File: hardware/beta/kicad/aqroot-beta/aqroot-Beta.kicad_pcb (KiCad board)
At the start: 4 copper layers, 74 x 155 mm, 188 parts, among them J1 CH280QV10-CT_50P, J2 Molex_5025700893, J3 USB_C_Receptacle_USB2.0_16P, J4 JST-PH-2 BATTERY, J5 COMMUNITY_HEADER_2x13, J6 JST-PH-2 SPEAKER, Q1 AO3400A, SW1 BOOT, SW2 UP, SW3 DOWN, SW4 LEFT, SW5 RIGHT, SW6 A_SELECT, SW7 B_BACK, SW8 HOME, SW9 SW_SPDT, U1 ESP32-S3-WROOM-1, U10 USBLC6-2SC6, U11 BQ25185, U12 TPS63020, U13 TPS61023, U14 MAX17048, U15 TPS22918, U16 TCA9517ADGK, U17 TPS61169DCKR, U2 TCA9535PWR, U3 TCA9535PWR, U4 BMI270, U5 MAX98357A, U6 TSOP38238, U7 E07-400M10S, U8 E22-900M22S, U9 ST25R3916-AQET

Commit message: route SX1262_RST_N from U2.5
Closes SX1262_RST_N: one island over U2.5, R13.1 and U8.15, 159.325 mm of
new copper in 17 tracks and 7 vias across In2 9 / B.Cu 8 / F.Cu 1. Board
ratsnest 414 -> 411, DRC 0 electrical errors. E5 x65 consumed in place.

The north-window architecture from the previous analysis pass held. The
source leaves U2.5 west on B.Cu, dives to In2 at x 13.700 to clear the
WAKE_INT_N B.Cu wall, returns to B.Cu at y 52.000 for the R13 pull-down
tee at x 17.375, hops F.Cu across x 23..30, then runs In2 east to x 57
and north to y 38.000. The band crossing is a B.Cu run at y 38.000 from
x 57 to x 71, well clear of both antenna bands, and the return descends
In2 down the east edge to meet the staged x65 crossing at y 85.000.
R13.2 is GND, so R13 is a pull-down tee and not a series element.

One correction to the audited geometry. The predicted 0.225 mm minimum
was scored against the 0.200 mm global clearance, but on the east lane
that gap falls against the USB_VBUS_CHG via at (70.775, 64.6), which
carries the elevated 0.250 mm VBUS_CHG routed clearance from .kicad_dru
section 10. At the audited x 71.500 the lane measured 0.225 mm and DRC
failed on exactly that one pair. The lane moved to x 71.600, the only
change against the audited route: the legal window is [71.525, 73.400]
and is empty of copper on In2 and of through vias, so the fix is a
0.100 mm lateral shift of three segments, not a new architecture. The
gap is now 0.325 mm and the board edge at x 74 is 2.300 mm away.

Actual minimum route clearance is 0.225 mm, at the x 13.700 y 52.000 via
against R10.1 on +3V3, where the requirement is the 0.200 mm global
figure. All four Edge.Cuts mounting cutouts were checked explicitly and
the nearest new copper is 12.082 mm from the hole at (70.5, 144.0).

RF audit: 0 new vias and 0 new outer-layer transit in either the 915 or
the 433 band, and no new In2 copper inside either band - the only in-band
copper on this net remains the pre-existing x65 segment, con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
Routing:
- net /SX1262_RST_N: track 32.0 -> 191.3 mm, vias 0 -> 7
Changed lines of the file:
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@@
 	(footprint "C_0603_1608Metric"
 		(layer "B.Cu")
-		(at 46.1 82.5)
+		(at 28.5 79 180)
 		(descr "Capacitor SMD 0603 (1608 Metric), square (rectangular) end terminal, IPC-7351 nominal, (Body size source: IPC-SM-782 page 76, https://www.pcb-3d.com/wordpress/wp-content/uploads/ipc-sm-782a_amendment_1_and_2.pdf)")
 		(tags "capacitor")
-		(property "Reference" "C56"
-			(at 0 1.43 180)
+		(property "Reference" "C13"
+			(at 0 1.43 0)
 			(layer "B.SilkS")
 			(effects
@@
 			)
 		)
-		(property "Value" "1uF"
-			(at 0 -1.43 180)
+		(property "Value" "100nF"
+			(at 0 -1.43 0)
 			(layer "B.Fab")
 			(effects
@@
 		)
 		(property "Datasheet" ""
-			(at 0 0 180)
+			(at 0 0 0)
 			(layer "B.Fab")
 			(hide yes)
@@
 		)
 		(property "Description" ""
-			(at 0 0 180)
+			(at 0 0 0)
 			(layer "B.Fab")
 			(hide yes)
@@
 		)
 		(property "KiLib_Generator" "SMD_2terminal_chip_molded"
-			(at 0 0 180)
+			(at 0 0 0)
 			(layer "B.SilkS")
 			(hide yes)
@@
 		(duplicate_pad_numbers_are_jumpers no)
 		(fp_line
-			(start -0.14058 -0.51)
-			(end 0.14058 -0.51)
+			(start -0.14058 0.51)
+			(end 0.14058 0.51)
 			(stroke
 				(width 0.12)
@@
 		)
 		(fp_line
-			(start -0.14058 0.51)
-			(end 0.14058 0.51)
+			(start -0.14058 -0.51)
+			(end 0.14058 -0.51)
 			(stroke
 				(width 0.12)
@@
 		)
 		(fp_text user "${REFERENCE}"
-			(at 0 0 180)
+			(at 0 0 0)
 			(layer "B.Fab")
 			(effects
@@
 		)
 		(pad "1" smd roundrect
-			(at -0.775 0)
+			(at -0.775 0 180)
 			(size 0.9 0.95)
 			(layers "B.Cu" "B.Mask" "B.Paste")
@@
 		)
 		(pad "2" smd roundrect
-			(at 0.775 0)
+			(at 0.775 0 180)
 			(size 0.9 0.95)
 			(layers "B.Cu" "B.Mask" "B.Paste")
@@
 	(footprint "C_0603_1608Metric"
 		(layer "B.Cu")
-		(at 28.5 79 180)
+		(at 46.1 82.5)
 		(descr "Capacitor SMD 0603 (1608 Metric), square (rectangular) end terminal, IPC-7351 nominal, (Body size source: IPC-SM-782 page 76, https://www.pcb-3d.com/wordpress/wp-content/uploads/ipc-sm-782a_amendment_1_and_2.pdf)")
 		(tags "capacitor")
-		(property "Reference" "C13"
-			(at 0 1.43 0)
+		(property "Reference" "C56"
+			(at 0 1.43 180)
 			(layer "B.SilkS")
 			(effects
@@
 			)
 		)
-		(property "Value" "100nF"
-			(at 0 -1.43 0)
+		(property "Value" "1uF"
+			(at 0 -1.43 180)
 			(layer "B.Fab")
 			(effects
@@
 		)
 		(property "Datasheet" ""
-			(at 0 0 0)
+			(at 0 0 180)
 			(layer "B.Fab")
 			(hide yes)
@@
 		)
 		(property "Description" ""
-			(at 0 0 0)
+			(at 0 0 180)
 			(layer "B.Fab")
 			(hide yes)
@@
 		)
 		(property "KiLib_Generator" "SMD_2terminal_chip_molded"
-			(at 0 0 0)
+			(at 0 0 180)
 			(layer "B.SilkS")
 			(hide yes)
@@
 		(duplicate_pad_numbers_are_jumpers no)
 		(fp_line
-			(start -0.14058 0.51)
-			(end 0.14058 0.51)
+			(start -0.14058 -0.51)
+			(end 0.14058 -0.51)
 			(stroke
 				(width 0.12)
@@
 		)
 		(fp_line
-			(start -0.14058 -0.51)
-			(end 0.14058 -0.51)
+			(start -0.14058 0.51)
+			(end 0.14058 0.51)
 			(stroke
 				(width 0.12)
@@
 		)
 		(fp_text user "${REFERENCE}"
-			(at 0 0 0)
+			(at 0 0 180)
 			(layer "B.Fab")
 			(effects
@@
 		)
 		(pad "1" smd roundrect
-			(at -0.775 0 180)
+			(at -0.775 0)
 			(size 0.9 0.95)
 			(layers "B.Cu" "B.Mask" "B.Paste")
@@
 		)
 		(pad "2" smd roundrect
-			(at 0.775 0 180)
+			(at 0.775 0)
 			(size 0.9 0.95)
 			(layers "B.Cu" "B.Mask" "B.Paste")
@@
 	)
 	(segment
+		(start 23 52)
+		(end 30 52)
+		(width 0.2)
+		(layer "F.Cu")
+		(net "/SX1262_RST_N")
+	)
+	(via
+		(at 13.7 48.35)
+		(size 0.6)
+		(drill 0.3)
+		(layers "F.Cu" "B.Cu")
+		(net "/SX1262_RST_N")
+	)
+	(via
+		(at 13.7 52)
+		(size 0.6)
+		(drill 0.3)
+		(layers "F.Cu" "B.Cu")
+		(net "/SX1262_RST_N")
+	)
+	(via
+		(at 23 52)
+		(size 0.6)
+		(drill 0.3)
+		(layers "F.Cu" "B.Cu")
+		(net "/SX1262_RST_N")
+	)
+	(via
+		(at 30 52)
+		(size 0.6)
+		(drill 0.3)
+		(layers "F.Cu" "B.Cu")
+		(net "/SX1262_RST_N")
+	)
+	(via
+		(at 57 38)
+		(size 0.6)
+		(drill 0.3)
+		(layers "F.Cu" "B.Cu")
+		(net "/SX1262_RST_N")
+	)
+	(via
+		(at 71 38)
+		(size 0.6)
+		(drill 0.3)
+		(layers "F.Cu" "B.Cu")
+		(net "/SX1262_RST_N")
+	)
+	(via
+		(at 65 131)
+		(size 0.6)
+		(drill 0.3)
+		(layers "F.Cu" "B.Cu")
+		(net "/SX1262_RST_N")
+	)
+	(segment
+		(start 9.7 44.975)
+		(end 11.5 44.975)
+		(width 0.2)
+		(layer "B.Cu")
+		(net "/SX1262_RST_N")
+	)
+	(segment
+		(start 11.5 44.975)
+		(end 11.5 48.35)
+		(width 0.2)
+		(layer "B.Cu")
+		(net "/SX1262_RST_N")
+	)
+	(segment
+		(start 11.5 48.35)
+		(end 13.7 48.35)
+		(width 0.2)
+		(layer "B.Cu")
+		(net "/SX1262_RST_N")
+	)
+	(segment
+		(start 13.7 52)
+		(end 23 52)
+		(width 0.2)
+		(layer "B.Cu")
+		(net "/SX1262_RST_N")
+	)
+	(segment
+		(start 17.375 52)
+		(end 17.375 53)
+		(width 0.2)
+		(layer "B.Cu")
+		(net "/SX1262_RST_N")
+	)
+	(segment
+		(start 57 38)
+		(end 71 38)
+		(width 0.2)
+		(layer "B.Cu")
+		(net "/SX1262_RST_N")
+	)
+	(segment
+		(start 65 131)
+		(end 65 131.8)
+		(width 0.2)
+		(layer "B.Cu")
+		(net "/SX1262_RST_N")
+	)
+	(segment
+		(start 65 131.8)
+		(end 58 131.8)
+		(width 0.2)
+		(layer "B.Cu")
+		(net "/SX1262_RST_N")
+	)
+	(segment
 		(start 65 85)
 		(end 65 117)
 		(width 0.2)
 		(layer "In2.Cu")
+		(net "/SX1262_RST_N")
+	)
+	(segment
+		(start 13.7 48.35)
+		(end 13.7 52)
+		(width 0.2)
+		(layer "In2.Cu")
+		(net "/SX1262_RST_N")
+	)
+	(segment
+		(start 30 52)
+		(end 57 52)
+		(width 0.2)
+		(layer "In2.Cu")
+		(net "/SX1262_RST_N")
+	)
+	(segment
+		(start 57 52)
+		(end 57 38)
+		(width 0.2)
+		(layer "In2.Cu")
+		(net "/SX1262_RST_N")
+	)
+	(segment
+		(start 71 38)
+		(end 71.6 38)
+		(width 0.2)
+		(layer "In2.Cu")
+		(net "/SX1262_RST_N")
+	)
+	(segment
+		(start 71.6 38)
+		(end 71.6 81.5)
+		(width 0.2)
+		(layer "In2.Cu")
+		(net "/SX1262_RST_N")
+	)
+	(segment
+		(start 71.6 81.5)
+		(end 65 81.5)
+		(width 0.2)
+		(layer "In2.Cu")
+		(net "/SX1262_RST_N")
+	)
+	(segment
+		(start 65 81.5)
+		(end 65 85)
+		(width 0.2)
+		(layer "In2.Cu")
+		(net "/SX1262_RST_N")
+	)
+	(segment
+		(start 65 117)
+		(end 65 131)
+		(width 0.2)
+		(layer "In2.Cu")

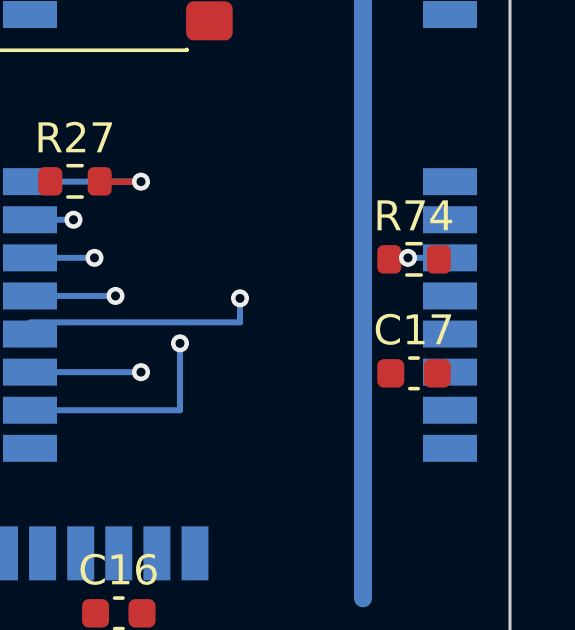
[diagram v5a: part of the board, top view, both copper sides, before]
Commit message: route DIO2_TXEN, closing SX1262 digital control
Closes DIO2_TXEN with a single B.Cu segment from U8.7 (72.000, 130.920)
to U8.8 (72.000, 132.190): 1.270 mm, 1 track, 0 vias, one layer. Board
ratsnest 411 -> 410, DRC 0 electrical errors.

Topology was taken from the current netlist rather than assumed. The net
is sheet-local, /04_SPI_B_RADIOS_NFC/DIO2_TXEN, and carries exactly two
pads: U8.7 and U8.8, adjacent on the east pad column at 1.27 mm pitch.
The schematic ties them with two DIO2_TXEN labels on separate stubs and
adds no pull-up, pull-down, series element or test branch, so the
minimum local connection is the direct pad-to-pad link and nothing more.
The track runs down the pad-column centreline at x 72.000, entirely
inside the two pads it joins.

Minimum clearance is 0.720 mm, symmetric against U8.6 on SX1262_RXEN
below and U8.9 on +3V3 above. Nearest neighbouring SX1262 net is
SX1262_RXEN, whose B.Cu escape and via at (70.6, 129.65) sit 1.165 mm
and 1.490 mm away. No via was introduced, the route never leaves the U8
pad area, no E5 lane was created and no RF corridor is crossed.

All nine SX1262 digital-control nets are now closed, each at ratsnest 0
and a single island: SPI_B_SCK, SPI_B_MOSI, SPI_B_MISO, SX1262_CS_N,
SX1262_BUSY, SX1262_DIO1, SX1262_RST_N, SX1262_RXEN and DIO2_TXEN.
Crossing lanes x62 CS_N, x63 DIO1, x64 BUSY, x65 RST_N and x66 RXEN are
all consumed. The C-E corridor still stages x67 CC1101_CS_N, x68
CC1101_GDO0 and x69.100 +3V3, plus BTN_HOME_N at x13.800 in C-W.

Tracks 540 -> 541, vias 145 -> 145, 0 removed, the single addition on
DIO2_TXEN under writer prefix 9c4e0000. 188 footprints unmoved, 0 pad net
assignments changed, 17 locked nets bit-identical. NFC_IRQ still 0 tracks
/ 0 vias / 0 zones, intentionally unconnected in Beta.

This pass also corrected a defect in the offline geometry checker used
for the audits. Its footprint rotation used a Y-up matrix and re-applied
the footprint angle to pads whose stored angle is already absolute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
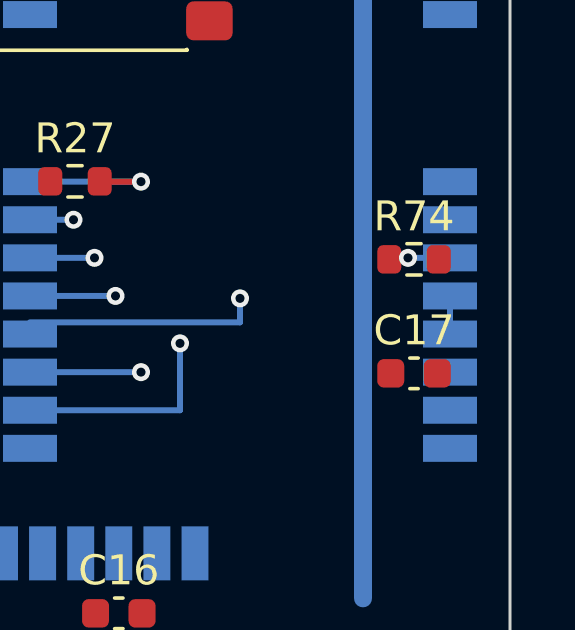
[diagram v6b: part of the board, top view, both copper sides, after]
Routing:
- net /04_SPI_B_RADIOS_NFC/DIO2_TXEN: track 0.00 -> 1.27 mm
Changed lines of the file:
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@@
 	(footprint "C_0603_1608Metric"
 		(layer "F.Cu")
-		(at 22.225 29.4 -90)
+		(at 22 26.9)
 		(descr "Capacitor SMD 0603 (1608 Metric), square (rectangular) end terminal, IPC-7351 nominal, (Body size source: IPC-SM-782 page 76, https://www.pcb-3d.com/wordpress/wp-content/uploads/ipc-sm-782a_amendment_1_and_2.pdf)")
 		(tags "capacitor")
-		(property "Reference" "C55"
-			(at 0 -1.43 270)
+		(property "Reference" "C50"
+			(at 0 -1.43 0)
 			(layer "F.SilkS")
 			(effects
@@
 			)
 		)
-		(property "Value" "2.2uF"
-			(at 0 1.43 270)
+		(property "Value" "10nF"
+			(at 0 1.43 0)
 			(layer "F.Fab")
 			(effects
@@
 		)
 		(property "Datasheet" ""
-			(at 0 0 270)
+			(at 0 0 0)
 			(layer "F.Fab")
 			(hide yes)
@@
 		)
 		(property "Description" ""
-			(at 0 0 270)
+			(at 0 0 0)
 			(layer "F.Fab")
 			(hide yes)
@@
 		)
 		(property "KiLib_Generator" "SMD_2terminal_chip_molded"
-			(at 0 0 270)
+			(at 0 0 0)
 			(layer "F.SilkS")
 			(hide yes)
@@
 		(duplicate_pad_numbers_are_jumpers no)
 		(fp_line
-			(start -0.14058 0.51)
-			(end 0.14058 0.51)
+			(start -0.14058 -0.51)
+			(end 0.14058 -0.51)
 			(stroke
 				(width 0.12)
@@
 		)
 		(fp_line
-			(start -0.14058 -0.51)
-			(end 0.14058 -0.51)
+			(start -0.14058 0.51)
+			(end 0.14058 0.51)
 			(stroke
 				(width 0.12)
@@
 		)
 		(fp_text user "${REFERENCE}"
-			(at 0 0 270)
+			(at 0 0 0)
 			(layer "F.Fab")
 			(effects
@@
 		)
 		(pad "1" smd roundrect
-			(at -0.775 0 270)
+			(at -0.775 0)
 			(size 0.9 0.95)
 			(layers "F.Cu" "F.Mask" "F.Paste")
 			(roundrect_rratio 0.25)
-			(net "/NFC_5V_PA_PENDING")
+			(net "/04_SPI_B_RADIOS_NFC/NFC_VDD_RF")
 		)
 		(pad "2" smd roundrect
-			(at 0.775 0 270)
+			(at 0.775 0)
 			(size 0.9 0.95)
 			(layers "F.Cu" "F.Mask" "F.Paste")
@@
 	(footprint "C_0603_1608Metric"
 		(layer "F.Cu")
-		(at 22 26.9)
+		(at 22.225 29.4 -90)
 		(descr "Capacitor SMD 0603 (1608 Metric), square (rectangular) end terminal, IPC-7351 nominal, (Body size source: IPC-SM-782 page 76, https://www.pcb-3d.com/wordpress/wp-content/uploads/ipc-sm-782a_amendment_1_and_2.pdf)")
 		(tags "capacitor")
-		(property "Reference" "C50"
-			(at 0 -1.43 0)
+		(property "Reference" "C55"
+			(at 0 -1.43 270)
 			(layer "F.SilkS")
 			(effects
@@
 			)
 		)
-		(property "Value" "10nF"
-			(at 0 1.43 0)
+		(property "Value" "2.2uF"
+			(at 0 1.43 270)
 			(layer "F.Fab")
 			(effects
@@
 		)
 		(property "Datasheet" ""
-			(at 0 0 0)
+			(at 0 0 270)
 			(layer "F.Fab")
 			(hide yes)
@@
 		)
 		(property "Description" ""
-			(at 0 0 0)
+			(at 0 0 270)
 			(layer "F.Fab")
 			(hide yes)
@@
 		)
 		(property "KiLib_Generator" "SMD_2terminal_chip_molded"
-			(at 0 0 0)
+			(at 0 0 270)
 			(layer "F.SilkS")
 			(hide yes)
@@
 		(duplicate_pad_numbers_are_jumpers no)
 		(fp_line
-			(start -0.14058 -0.51)
-			(end 0.14058 -0.51)
+			(start -0.14058 0.51)
+			(end 0.14058 0.51)
 			(stroke
 				(width 0.12)
@@
 		)
 		(fp_line
-			(start -0.14058 0.51)
-			(end 0.14058 0.51)
+			(start -0.14058 -0.51)
+			(end 0.14058 -0.51)
 			(stroke
 				(width 0.12)
@@
 		)
 		(fp_text user "${REFERENCE}"
-			(at 0 0 0)
+			(at 0 0 270)
 			(layer "F.Fab")
 			(effects
@@
 		)
 		(pad "1" smd roundrect
-			(at -0.775 0)
+			(at -0.775 0 270)
 			(size 0.9 0.95)
 			(layers "F.Cu" "F.Mask" "F.Paste")
 			(roundrect_rratio 0.25)
-			(net "/04_SPI_B_RADIOS_NFC/NFC_VDD_RF")
+			(net "/NFC_5V_PA_PENDING")
 		)
 		(pad "2" smd roundrect
-			(at 0.775 0)
+			(at 0.775 0 270)
 			(size 0.9 0.95)
 			(layers "F.Cu" "F.Mask" "F.Paste")
@@
 	)
 	(segment
+		(start 72 130.92)
+		(end 72 132.19)
+		(width 0.2)
+		(layer "B.Cu")
+		(net "/04_SPI_B_RADIOS_NFC/DIO2_TXEN")
+	)
+	(segment

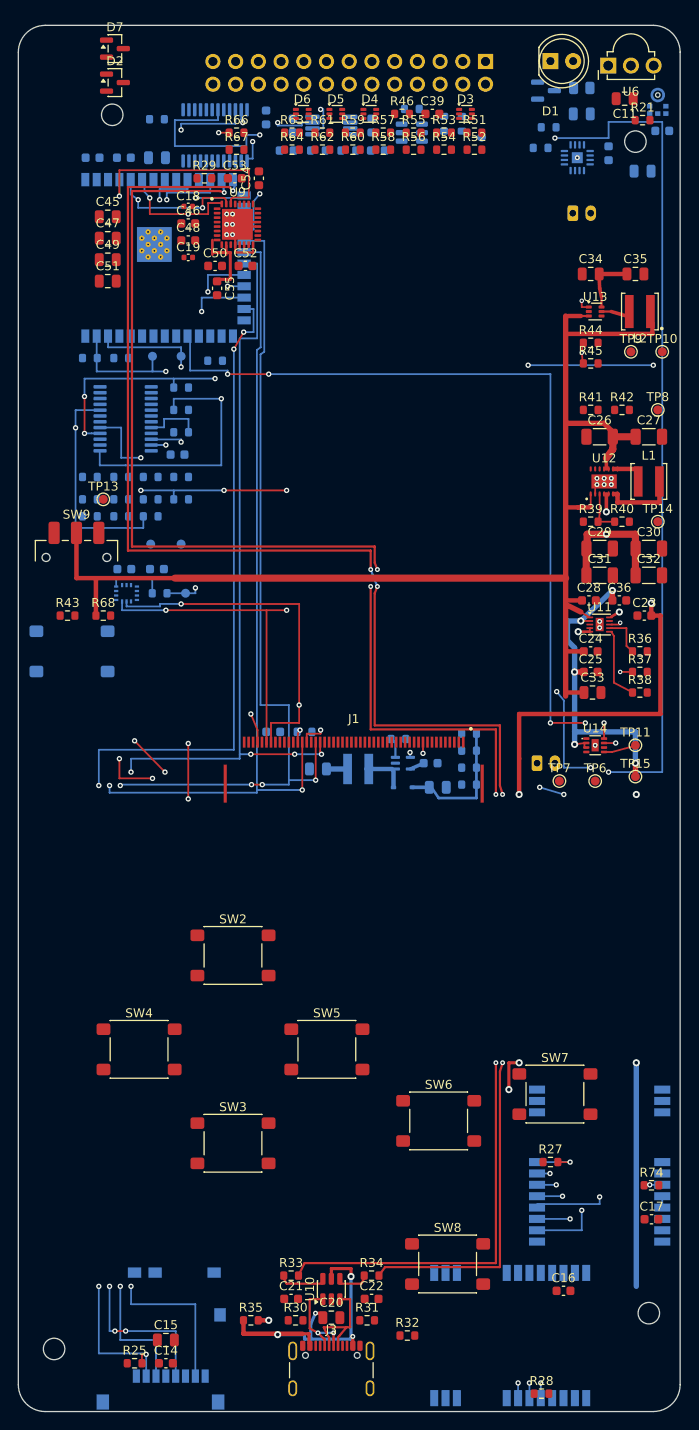
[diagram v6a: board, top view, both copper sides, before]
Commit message: route CC1101_CS_N and CC1101_GDO0, closing radio digital control
Closes both CC1101 control nets. CS_N: one island over U1.7, R28.2 and
U7.19, 168.078 mm of new copper in 16 tracks and 5 vias. GDO0: one island
over U1.8 and U7.15, 166.487 mm in 24 tracks and 7 vias. Board ratsnest
410 -> 405, DRC 0 electrical errors. E5 x67 and x68 consumed in place.

Topology was re-read from the current netlist. R28.1 is +3V3 and R28.2 is
CC1101_CS_N, so R28 is a pull-up tee and the trunk does NOT pass through
it; R28.2 is the only F.Cu terminal on either net. GDO0 carries exactly
two pads, U1.8 and U7.15, with no pull resistor and no test point.

CS_N was routed first because it is the more constrained net: it has three
terminals against GDO0's two, it lands at U7.19 on the far side of the
already-routed SPI-B escape fan, and at the U1 end both nets want the same
0.25 mm B.Cu slot at x 15.35-15.60 - the only gap between the C3 pads and
the SX1262_CS_N/BUSY escape walls. CS_N takes that slot and GDO0 uses the
eastern one at x 17.30.

Both escape north out of U1's pad row rather than south under the module,
because the via fence at y 19.1-19.5 leaves only a 0.5 mm gap between the
SPI_B_MISO and SX1262_CS_N vias - too narrow for a 0.2 mm track needing
0.2 mm clearance. They then take the single free F.Cu east corridor at
y 14.700, descend west of NFC RESERVED, and cross the mid-board on F.Cu
and B.Cu before entering their staged In2 lanes at y 85.

The R28 tee leaves the trunk at (63.500,143.000), well north of the SPI-B
escape fan: the three SPI-B vias at y 151.800 sit on 1.27 mm pitch and
their In2 verticals leave a 0.07 mm window between them, so no via fits
south of them and the crossing is made on F.Cu instead.

Minimum clearance is 0.225 mm on CS_N, against R67 and C54 on the F.Cu
corridor, and 0.200 mm on GDO0 at four via-to-track pairs that sit exactly
on the global figure. The CS_N trunk threads the 0.800 mm gap between the
J4 battery-connector pads centred at x 59.000, giv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
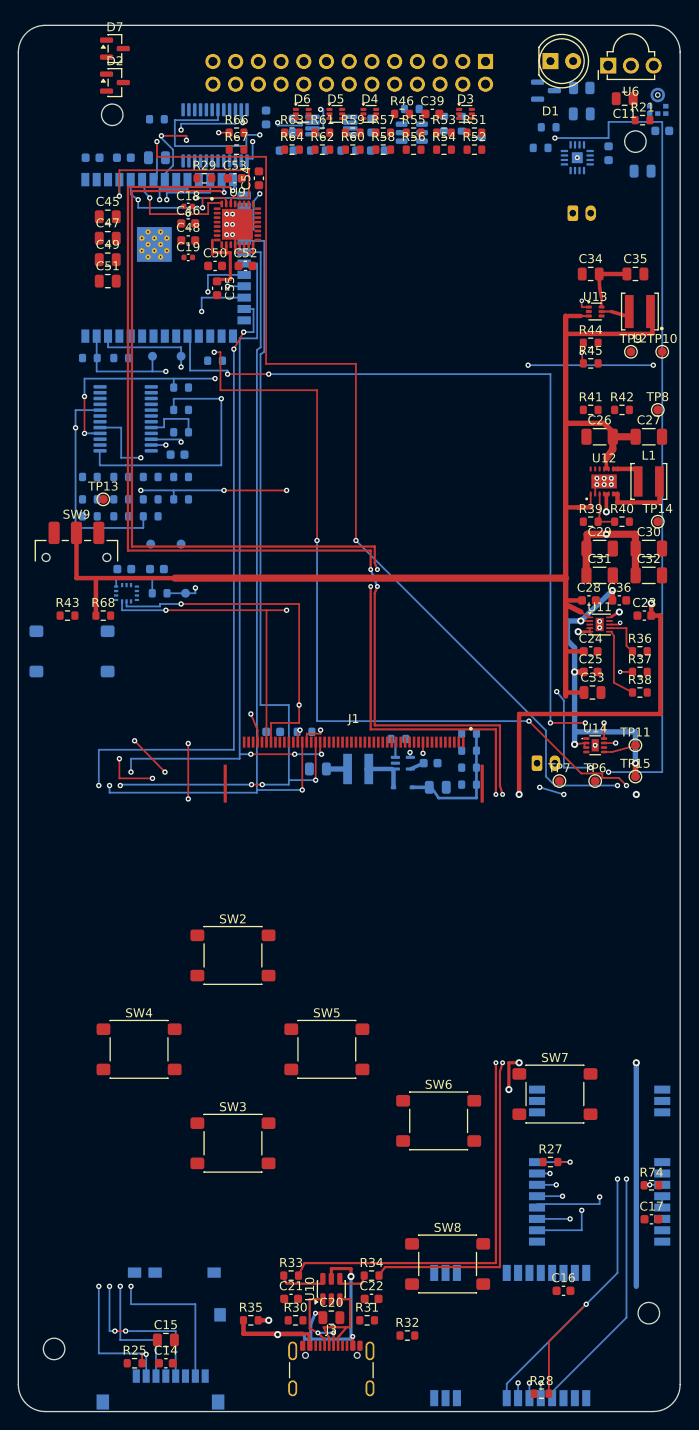
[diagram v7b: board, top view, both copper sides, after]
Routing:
- net /CC1101_CS_N: track 32.0 -> 200.1 mm, vias 0 -> 5
- net /CC1101_GDO0: track 32.0 -> 198.5 mm, vias 0 -> 7
